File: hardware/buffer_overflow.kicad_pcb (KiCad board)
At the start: 2 copper layers, 37.5 x 48.3 mm, 30 parts, among them J1 In, J2 Out, J3 +, J4 FS, J5 In_G, J6 Out_G, J7 -, J8 FS_G, U1 LM741

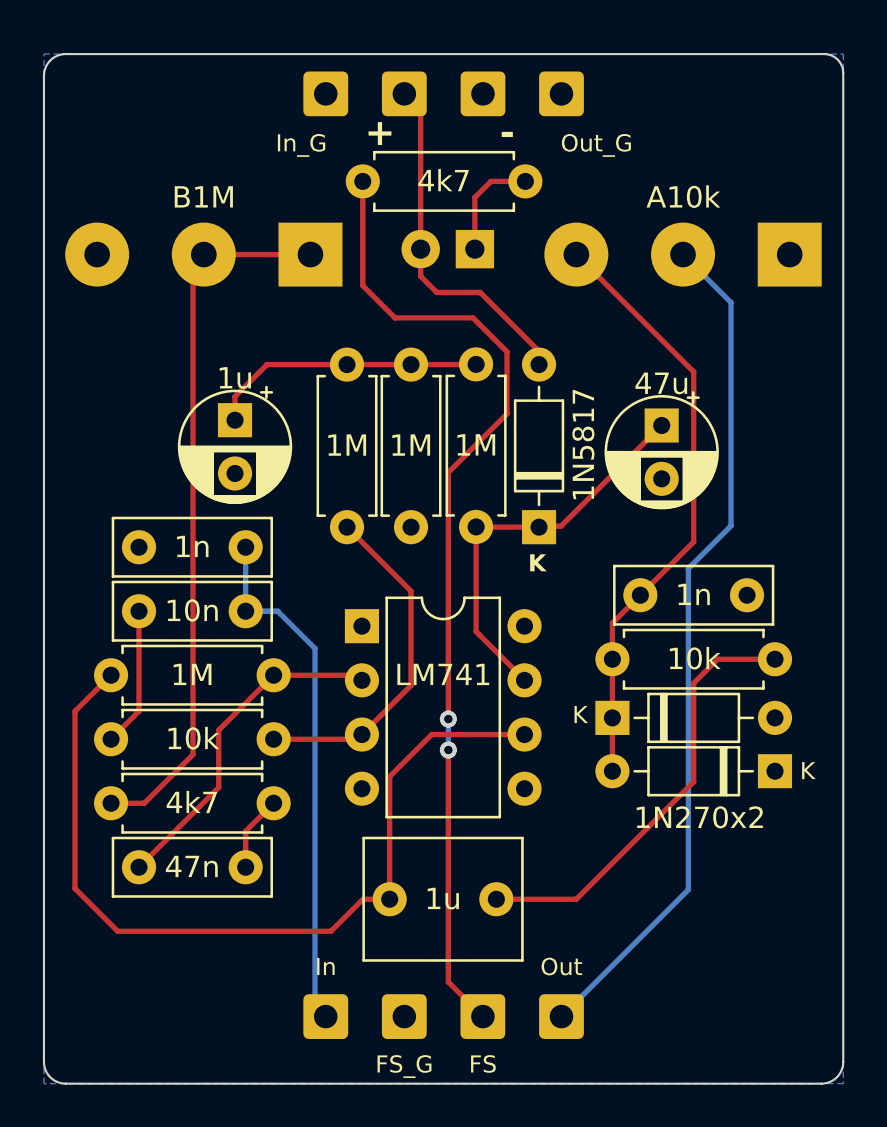
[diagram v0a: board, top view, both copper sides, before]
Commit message: Updates for v0.30:  - Replace wire connections with molex picoblade connectors  - Many cosmetic changes and layout changes to reduce size and improve appearance
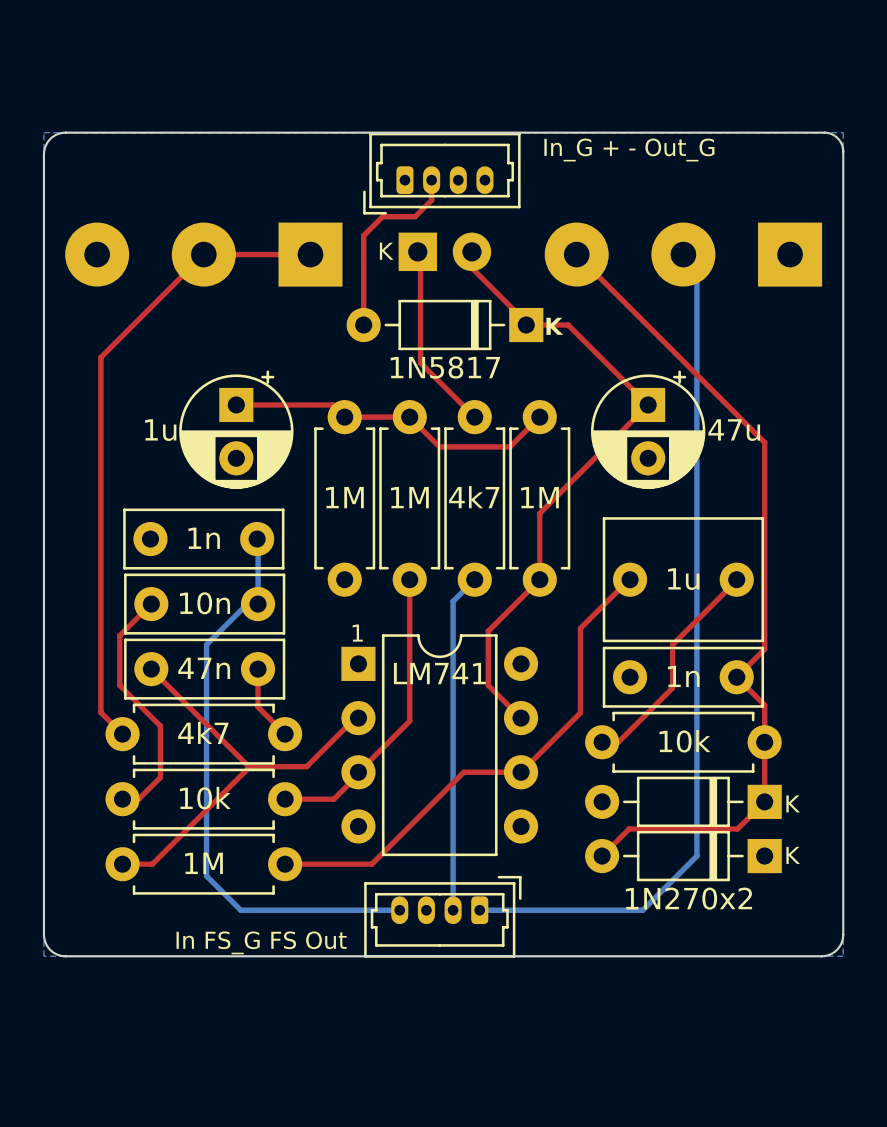
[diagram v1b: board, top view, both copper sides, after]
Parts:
- removed J3: +, Connector_Wire:SolderWire-0.5sqmm_1x01_D0.9mm_OD2.1mm
- removed J4: FS, Connector_Wire:SolderWire-0.5sqmm_1x01_D0.9mm_OD2.1mm
- removed J5: In_G, Connector_Wire:SolderWire-0.5sqmm_1x01_D0.9mm_OD2.1mm
- removed J6: Out_G, Connector_Wire:SolderWire-0.5sqmm_1x01_D0.9mm_OD2.1mm
- removed J7: -, Connector_Wire:SolderWire-0.5sqmm_1x01_D0.9mm_OD2.1mm
- removed J8: FS_G, Connector_Wire:SolderWire-0.5sqmm_1x01_D0.9mm_OD2.1mm
- J1: value In -> Upper Connector; footprint Connector_Wire:SolderWire-0.5sqmm_1x01_D0.9mm_OD2.1mm -> Connector_Molex:Molex_PicoBlade_53047-0410_1x04_P1.25mm_Vertical
- J2: value Out -> Lower Connector; footprint Connector_Wire:SolderWire-0.5sqmm_1x01_D0.9mm_OD2.1mm -> Connector_Molex:Molex_PicoBlade_53047-0410_1x04_P1.25mm_Vertical
- moved J1 39.4 mm to (59.5, 30.3)
- moved C6 18.7 mm to (70.0, 49.0)
- moved R7 12.0 mm to (53.8, 62.4), turned to 180 degrees
- moved R1 11.3 mm to (62.7, 41.4), turned to -90 degrees
- moved D1 9.49 mm to (65.2, 37.1), turned to 180 degrees
- moved C4 9.30 mm to (52.6, 53.2)
- moved D4 8.15 mm to (76.3, 59.4), turned to 180 degrees
- moved R8 8.13 mm to (76.3, 56.6), turned to 180 degrees
- moved C7 6.70 mm to (70.0, 53.6), turned to 0 degrees
- moved J2 6.29 mm to (63.0, 64.5), turned to 180 degrees
- moved D3 4.01 mm to (76.3, 62.0)
- moved R5 3.96 mm to (56.6, 49.0)
- moved R4 3.88 mm to (65.8, 41.4)
- moved R3 3.83 mm to (59.7, 49.0)
- moved R6 3.28 mm to (53.8, 56.3)
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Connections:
- D2 pad 2: /DC_SHIELD -> 9V
- J1 pad 1: /INPUT_TIP -> GND
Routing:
- net /Footswitch: track 45.9 -> 15.9 mm, vias 2 -> 0
- net /741_OUT: track 39.7 -> 24.0 mm
- net 9V: track 18.8 -> 30.2 mm
- net /PRE_VOLUME: track 28.1 -> 39.1 mm
- net Net-(C6-Pad2): track 20.4 -> 10.7 mm
- net /DC_SHIELD: track 17.8 -> 9.00 mm
- net Net-(C3-Pad2): track 6.54 -> 11.7 mm
- net /741_Inv: track 15.9 -> 20.4 mm
- net /GAIN_CTL: track 34.2 -> 29.9 mm
- net Net-(D2-K): track 5.10 -> 8.80 mm
- net VREF: track 13.0 -> 15.6 mm
- net /INPUT_TIP: track 24.4 -> 26.8 mm
- net /741_NonInv: track 16.1 -> 14.0 mm
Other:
- board size 37.5 x 48.3 mm -> 37.5 x 38.6 mm

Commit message: Offload functions of "noise floor" interface boards for v0.35
 - more layout changes coming, but functionality should be the same.
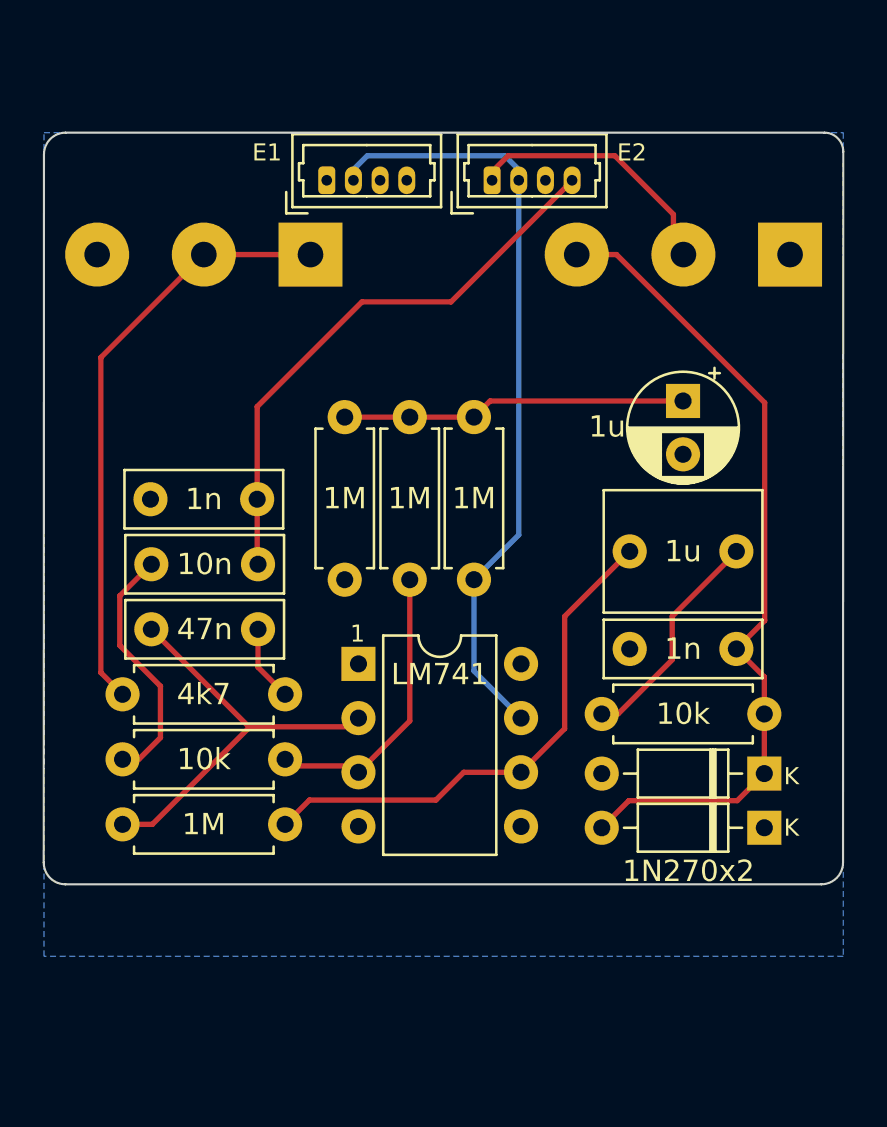
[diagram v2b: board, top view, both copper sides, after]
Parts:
- removed C2: 47u, Capacitor_THT:CP_Radial_D5.0mm_P2.50mm
- removed D1: 1N5817, Diode_THT:D_DO-35_SOD27_P7.62mm_Horizontal
- removed D2: On, LED_THT:LED_D3.0mm
- removed R1: 4k7, Resistor_THT:R_Axial_DIN0207_L6.3mm_D2.5mm_P7.62mm_Horizontal
- J1: value Upper Connector -> E1
- J2: value Lower Connector -> E2
- moved J2 34.2 mm to (63.5, 30.3), turned to 0 degrees
- moved C5 20.9 mm to (72.5, 40.6)
- moved J1 3.67 mm to (55.8, 30.3)
- moved R4 3.09 mm to (62.7, 41.4)
- moved C4 1.87 mm to (52.6, 51.3)
- moved R6 1.87 mm to (53.8, 54.4)
- moved C1 1.87 mm to (47.5, 45.2)
- moved C3 1.87 mm to (52.6, 48.3)
- moved R2 1.87 mm to (46.2, 57.4)
- moved R7 1.87 mm to (53.8, 60.5)
- moved C6 1.33 mm to (70.0, 47.7)
- moved C7 1.33 mm to (70.0, 52.3)
- moved D3 1.33 mm to (76.3, 60.6)
- moved D4 1.33 mm to (76.3, 58.1)
- moved R8 1.33 mm to (76.3, 55.3)
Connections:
- net /INPUT_TIP renamed /EFFECT_IN
- net /OUTPUT_TIP renamed /EFFECT_OUT
- J1 pad 1: GND -> unconnected-(J1-Pin_1-Pad1)
- J1 pad 2: /DC_SHIELD -> /9V0
- J1 pad 3: GND -> unconnected-(J1-Pin_3-Pad3)
- J1 pad 4: GND -> unconnected-(J1-Pin_4-Pad4)
- J2 pad 2: /Footswitch -> /9V0
- R4 pad 2: 9V -> /9V0
- U1 pad 7: 9V -> /9V0
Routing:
- net /9V0: track 0.00 -> 36.3 mm
- net 9V: track 30.2 -> 0.00 mm
- net /EFFECT_OUT: track 39.7 -> 12.4 mm
- net /Footswitch: track 15.9 -> 0.00 mm
- net /DC_SHIELD: track 9.00 -> 0.00 mm
- net Net-(D2-K): track 8.80 -> 0.00 mm
- net /GAIN_CTL: track 29.9 -> 28.0 mm
- net /741_Inv: track 20.4 -> 19.6 mm
- net /741_NonInv: track 14.0 -> 13.3 mm
- net VREF: track 15.6 -> 16.2 mm
- net /741_OUT: track 24.0 -> 24.5 mm
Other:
- board size 37.5 x 38.6 mm -> 37.5 x 35.2 mm

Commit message: condense and optimize layout
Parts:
- moved R7 24.4 mm to (60.1, 36.9), turned to -90 degrees
- moved C5 21.2 mm to (51.5, 38.0), turned to 180 degrees
- moved D3 19.5 mm to (68.9, 42.6), turned to 0 degrees
- moved D4 18.0 mm to (76.6, 40.1)
- moved R6 7.76 mm to (46.7, 51.4), turned to 0 degrees
- moved C7 6.83 mm to (70.5, 45.5)
- moved U1 5.83 mm to (57.8, 47.2)
- moved R3 5.72 mm to (63.2, 44.5)
- moved C4 5.64 mm to (47.8, 48.4), turned to 0 degrees
- moved R4 4.68 mm to (66.2, 44.5), turned to 90 degrees
- moved R5 4.55 mm to (57.1, 44.5)
- moved POT2 4.08 mm to (54.1, 29.6)
- moved POT1 3.57 mm to (69.0, 29.6)
- moved R2 3.03 mm to (46.7, 54.4)
- moved C1 3.00 mm to (47.8, 42.3)
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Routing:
- net /741_Inv: track 19.6 -> 12.3 mm
- net /PRE_VOLUME: track 38.8 -> 31.7 mm
- net VREF: track 16.2 -> 22.0 mm
- net /9V0: track 36.3 -> 31.1 mm
- net /EFFECT_IN: track 26.6 -> 31.3 mm
- net /GAIN_CTL: track 28.0 -> 23.4 mm
- net Net-(C6-Pad2): track 10.7 -> 8.32 mm
- net /EFFECT_OUT: track 12.4 -> 10.5 mm
- net /741_NonInv: track 13.3 -> 14.4 mm
- net Net-(C3-Pad2): track 11.7 -> 10.8 mm
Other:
- board size 37.5 x 35.2 mm -> 33.1 x 29.9 mm
